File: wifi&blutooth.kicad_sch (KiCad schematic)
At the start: 35 parts, among them Q5 2SK3018, U23 BGS12P2L6E6327XTSA1, U24 AP6256, Y2 ???

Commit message: Add files via upload
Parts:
- removed F1, F2: Polyfuse_Small, symbol Device:Polyfuse_Small
- removed JP1: SolderJumper_3_Open, Jumper:SolderJumper-3_P1.3mm_Open_RoundedPad1.0x1.5mm_NumberLabels, symbol Jumper:SolderJumper_3_Open
- removed R76, R85: 0R, PCM_Resistor_SMD_AKL:R_0402_1005Metric, symbol Device:R_Small
- removed R82: 10k, PCM_Resistor_SMD_AKL:R_0402_1005Metric, symbol Device:R_Small
- added R116, R117: 0R, PCM_Resistor_SMD_AKL:R_0402_1005Metric_Pad0.72x0.64mm, symbol Device:R_Small
- added R140: 10k, PCM_Resistor_SMD_AKL:R_0402_1005Metric, symbol Device:R_Small
- C336: renamed from C135; value 100n -> 1u
- C338: renamed from C137; value 100n -> 1u
- C339: renamed from C138; value 100n -> 1u
- C345: renamed from C144; value ??? -> 10pF
- C346: renamed from C145; value ??? -> 10pF
- Y5: renamed from Y2; value ??? -> T3225374MDBDE2X
- renumbered C136 to C337, C139 to C340, C140 to C341, C141 to C342, C142 to C343, C143 to C344, L2 to L13, L3 to L14, LED1 to LED3, Q5 to Q6, R77 to R135, R78 to R136, R79 to R137, R80 to R138, R81 to R139, R83 to R141, R84 to R142, R86 to R144, R87 to R145, U23 to U27, U24 to U28
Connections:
- net +1.8V: no longer C336.1, C337.1, U28.22 (VDDIO)
- net +3.3V: no longer C339.1, C340.1, U28.9 (VBAT)
- net SDIO_VSWL: now also R140.2
- net at C341.1, U27.1 (RF2): now also R116.1
- net at AE1.1 (A), C342.1: now also R116.2
- net at C343.1, U27.3 (RF1): now also R117.1
- net at AE2.1 (A), L13.1: now also R117.2
- net BT_HOST_WAKE renamed BT_WAKE_HOST_H
- net BT_REG_ON renamed BT_REG_ON_H
- net BT_WAKE renamed HOST_WAKE_BT_H
- net PCM_CLK renamed SAI2_SCLK_M0
- net PCM_IN renamed SAI2_SDO_M0
- net PCM_OUT renamed SAI2_SDI_M0
- net PCM_SYNC renamed SAI2_LRCK_M0
- net SDIO_CLK renamed SDMMC1_CLK_M0
- net SDIO_CMD renamed SDMMC1_CMD_M0
- net SDIO_D0 renamed SDMMC1_D0_M0
- net SDIO_D1 renamed SDMMC1_D1_M0
- net SDIO_D2 renamed SDMMC1_D2_M0
- net SDIO_D3 renamed SDMMC1_D3_M0
- net UART_CST renamed UART4_RTSN_M1
- net UART_RST renamed UART4_CTSN_M1
- net UART_RX renamed UART4_RX_M1
- net UART_TX renamed UART4_TX_M1
- net WIIFI_HOST_WAKE renamed WIFI_WAKE_HOST_H
- net WIIFI_REG_ON renamed WIFI_REG_ON_H
- new net VCC_1V8_S3: C336.1, C337.1, R140.1, U28.22 (VDDIO)
- new net VCC_3V3_S0: C339.1, C340.1, U28.9 (VBAT)
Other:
- note added: "I Need To search about it"
- moved on the sheet: AE1, AE2, C336, C337, C338, C339, C340, C341, C342, C343, C344, C345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

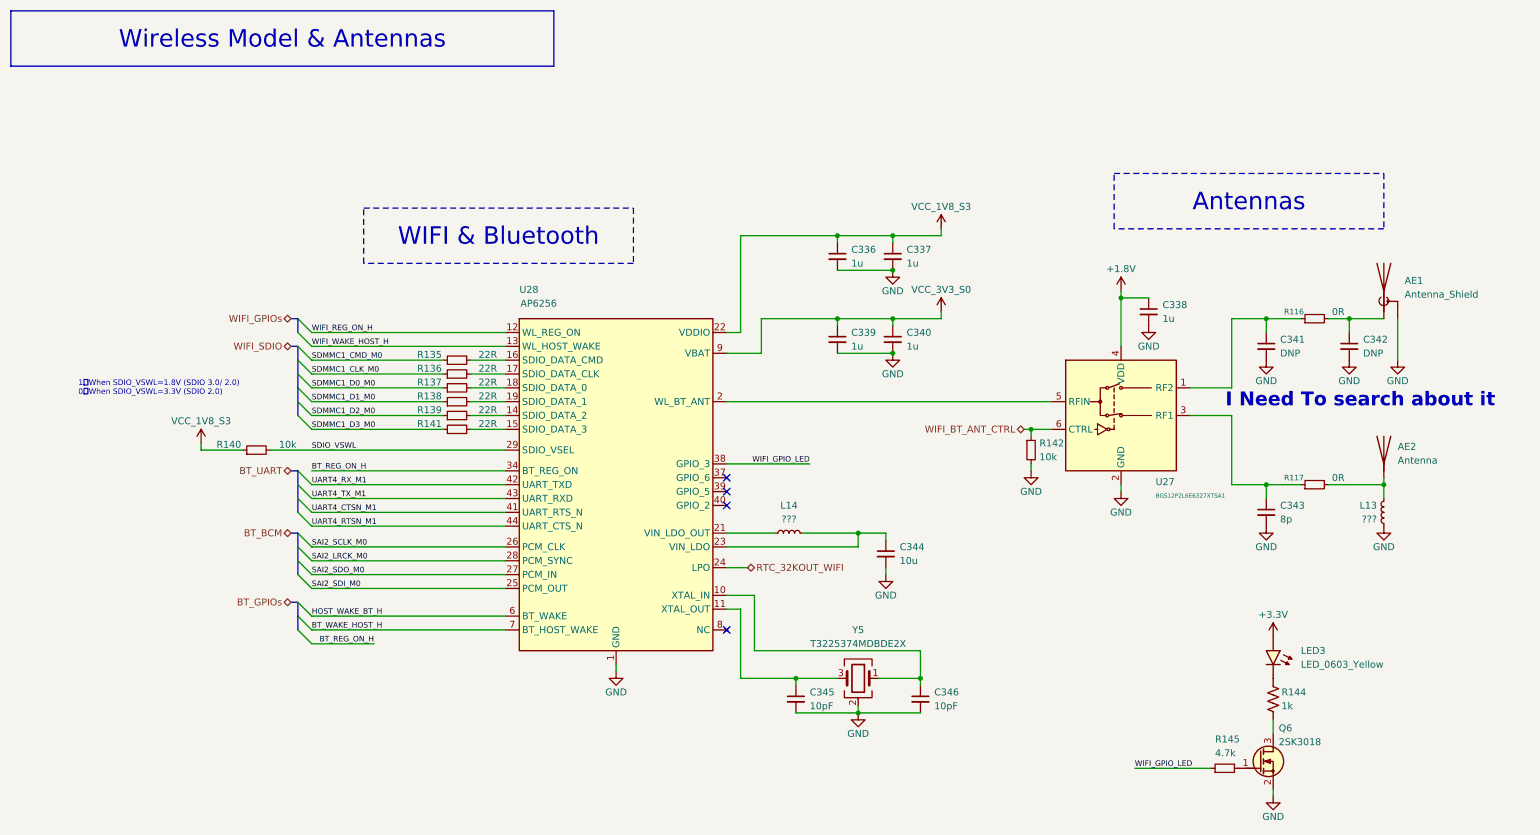
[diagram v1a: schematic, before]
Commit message: SBC Board V0.2
The SBC schematics before footprint and part number check
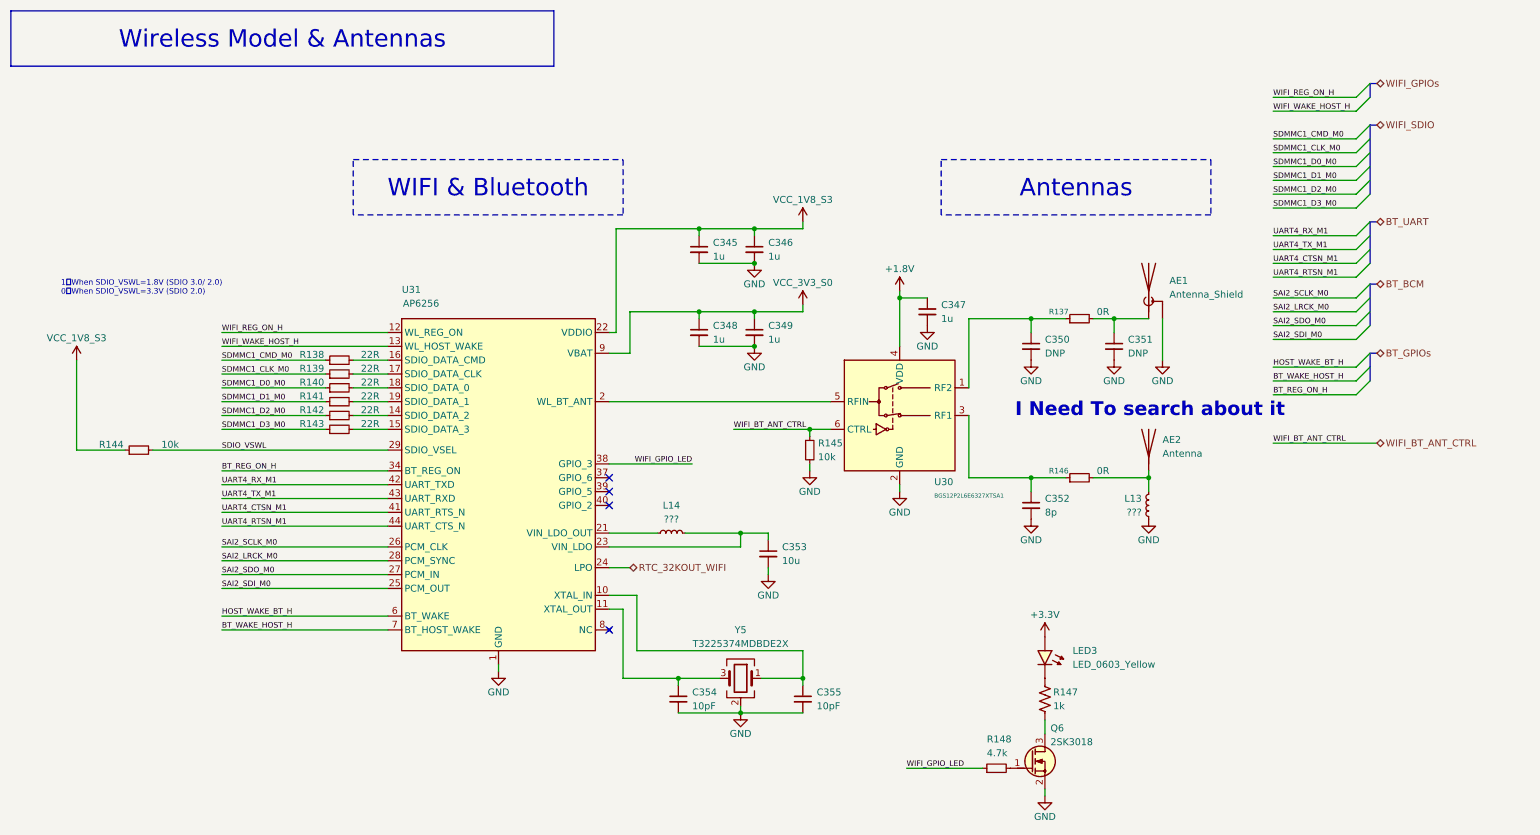
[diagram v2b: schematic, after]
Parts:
- renumbered C336 to C345, C337 to C346, C338 to C347, C339 to C348, C340 to C349, C341 to C350, C342 to C351, C343 to C352, C344 to C353, C345 to C354, C346 to C355, R116 to R137, R135 to R138, R136 to R139, R137 to R140, R138 to R141, R139 to R142, R141 to R143, R140 to R144, R142 to R145, R117 to R146, R144 to R147, R145 to R148, U27 to U30, U28 to U31
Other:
- moved on the sheet: AE1, AE2, C345, C346, C347, C348, C349, C350, C351, C352, C353, C354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

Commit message: SBCv0.3
there is no big thing update just some LCSC & Mouser parts
and Big problem deleted alot of component values (:
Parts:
- removed C352: 8p, Capacitor_SMD:C_0402_1005Metric_Pad0.74x0.62mm_HandSolder, symbol New_Library_0:C_Small_edited
- removed C354, C355: 10pF, Capacitor_SMD:C_0402_1005Metric_Pad0.74x0.62mm_HandSolder, symbol New_Library_0:C_Small_edited
- added C305: 10u, Capacitor_SMD:C_0603_1608Metric, symbol New_Library_0:C_Small_edited
- added C307, C311: 12pF, Capacitor_SMD:C_0402_1005Metric_Pad0.74x0.62mm_HandSolder, symbol New_Library_0:C_Small_edited
- AE1: value Antenna_Shield -> ufl connector; LCSC Part (none) -> C5137195
- AE2: value Antenna -> W3006; footprint (none) -> Datasheet_Footprints:Pulse_W3006_10x3.2mm; LCSC Part (none) -> C5123155; Mouser Part (none) -> 673-W3006
- C345, C347, C348: LCSC Part (none) -> C5209398; Mouser Part (none) -> CL03A105KP3NSNC
- C346, C349: footprint Capacitor_SMD:C_0402_1005Metric_Pad0.74x0.62mm_HandSolder -> Capacitor_SMD:C_0201_0603Metric_Pad0.64x0.40mm_HandSolder; LCSC Part (none) -> C5209398; Mouser Part (none) -> CL03A105KP3NSNC
- C350, C351: now not fitted
- C353: value 10u -> DNP; footprint Capacitor_SMD:C_0201_0603Metric -> Capacitor_SMD:C_0402_1005Metric_Pad0.74x0.62mm_HandSolder; now not fitted
- L13, L14: LCSC Part (none) -> (show_name no)
- LED3: Mouser Part (none) -> (font (size 1.27 1.27))
- R137, R146: value 0R -> (none); LCSC Part (none) -> )
- R138, R139, R140, R141, R142, R143: value 22R -> (none); LCSC Part (none) -> (do_not_autoplace no)
- R144, R145: LCSC Part (none) -> (at 0 0 0)
- R147: value 1k -> (none); LCSC Part (none) -> (effects
- R148: value 4.7k -> (none); LCSC Part (none) -> (show_name no)
- U30: value BGS12P2L6E6327XTSA1 -> (none); Mouser Part (none) -> (length 2.032)
- U31: value AP6256 -> AP2553W6-7; footprint (none) -> Package_TO_SOT_SMD:SOT-23-6_Handsoldering; LCSC Part (none) -> C212302; Mouser Part (none) -> 621-AP2553W6-7
- Y5: value T3225374MDBDE2X -> (none); Mouser Part (none) -> )
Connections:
- net GND: now also C305.2, C307.2, C311.2
- net at U31.10 (XTAL_IN), Y5.1: now also C311.1
- net at U31.11 (XTAL_OUT), Y5.3: now also C307.1
- net at L14.2, U31.23 (VIN_LDO): now also C305.1; no longer C353.1
- net at R146.1, U30.3 (RF1): now also C353.1

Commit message: SBCv0.4
add LCSC & Mouser parts 
and solve the deleted value in the past version
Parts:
- removed R138, R139, R140, R141, R142, R143: (no value), PCM_Resistor_SMD_AKL:R_0402_1005Metric, symbol Device:R_Small
- removed R147: (no value), PCM_Resistor_SMD_AKL:R_0402_1005Metric, symbol Device:R_US
- added R117: 1k, PCM_Resistor_SMD_AKL:R_0402_1005Metric, symbol Device:R_Small
- added R175, R176, R183, R188, R247, R248: 22R, PCM_Resistor_SMD_AKL:R_0402_1005Metric, symbol Device:R_Small
- AE1: value ufl connector -> BWU.FL-IPEX1
- L13: value ??? -> LQW15AN1N5B00D; footprint Inductor_SMD:L_1008_2520Metric -> Inductor_SMD:L_0402_1005Metric; LCSC Part (show_name no) -> C18221
- L14: value ??? -> 3.3; footprint Inductor_SMD:L_1008_2520Metric -> Inductor_SMD:L_Coilcraft_0805HQ_2012Metric; LCSC Part (show_name no) -> C2926398
- LED3: value LED_0603_Yellow -> XL-1608UYC-06; LCSC Part (none) -> C965802; Mouser Part (font (size 1.27 1.27)) -> (none)
- Q6: LCSC Part (none) -> C20069148
- R137, R146: value (none) -> 0R; footprint PCM_Resistor_SMD_AKL:R_0402_1005Metric_Pad0.72x0.64mm -> PCM_Resistor_SMD_AKL:R_0402_1005Metric; LCSC Part ) -> C106231; Mouser Part (none) -> 603-RC0402FR-070RL
- R144, R145: LCSC Part (at 0 0 0) -> C60490; Mouser Part (none) -> 603-RC0402FR-0710KL
- R148: value (none) -> 4.7k; LCSC Part (show_name no) -> C105871; Mouser Part (none) -> 603-RC0402FR-074K7L
- U30: value (none) -> BGS12WN6E6327; LCSC Part (none) -> C534203; Mouser Part (length 2.032) -> 726-BGS12WN6E6327XTS
- U31: value AP2553W6-7 -> AP6256; footprint Package_TO_SOT_SMD:SOT-23-6_Handsoldering -> Datasheet_Footprints:QFN-44_L12.0-W12.0-P0.90-TL_AP6256; LCSC Part C212302 -> C5248079
- Y5: value (none) -> T3225374MDBDE2X; LCSC Part (none) -> C20885046; Mouser Part ) -> (none)
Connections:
- net SDMMC1_CLK_M0: now also R176.1
- net SDMMC1_CMD_M0: now also R175.1
- net SDMMC1_D0_M0: now also R183.1
- net SDMMC1_D1_M0: now also R188.1
- net SDMMC1_D2_M0: now also R247.1
- net SDMMC1_D3_M0: now also R248.1
- net at U31.14 (SDIO_DATA_2): now also R247.2
- net at U31.15 (SDIO_DATA_3): now also R248.2
- net at U31.16 (SDIO_DATA_CMD): now also R175.2
- net at U31.17 (SDIO_DATA_CLK): now also R176.2
- net at U31.18 (SDIO_DATA_0): now also R183.2
- net at U31.19 (SDIO_DATA_1): now also R188.2
- net at Q6.3 (D): now also R117.2
- net at LED3.1 (K): now also R117.1
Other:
- moved on the sheet: C350, C351, C353
